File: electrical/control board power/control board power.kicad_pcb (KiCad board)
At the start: 2 copper layers, 147.3 x 147.3 mm, 67 parts, among them J1 Conn_01x02, J10 48V_from_conversion, J11 Aux_2, J17 Switch_B, J2 5V, J3 Barrel_Jack, J4 Switch_A, J5 Switch_Input, J6 Power_Connector, J7 Switch_A_High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

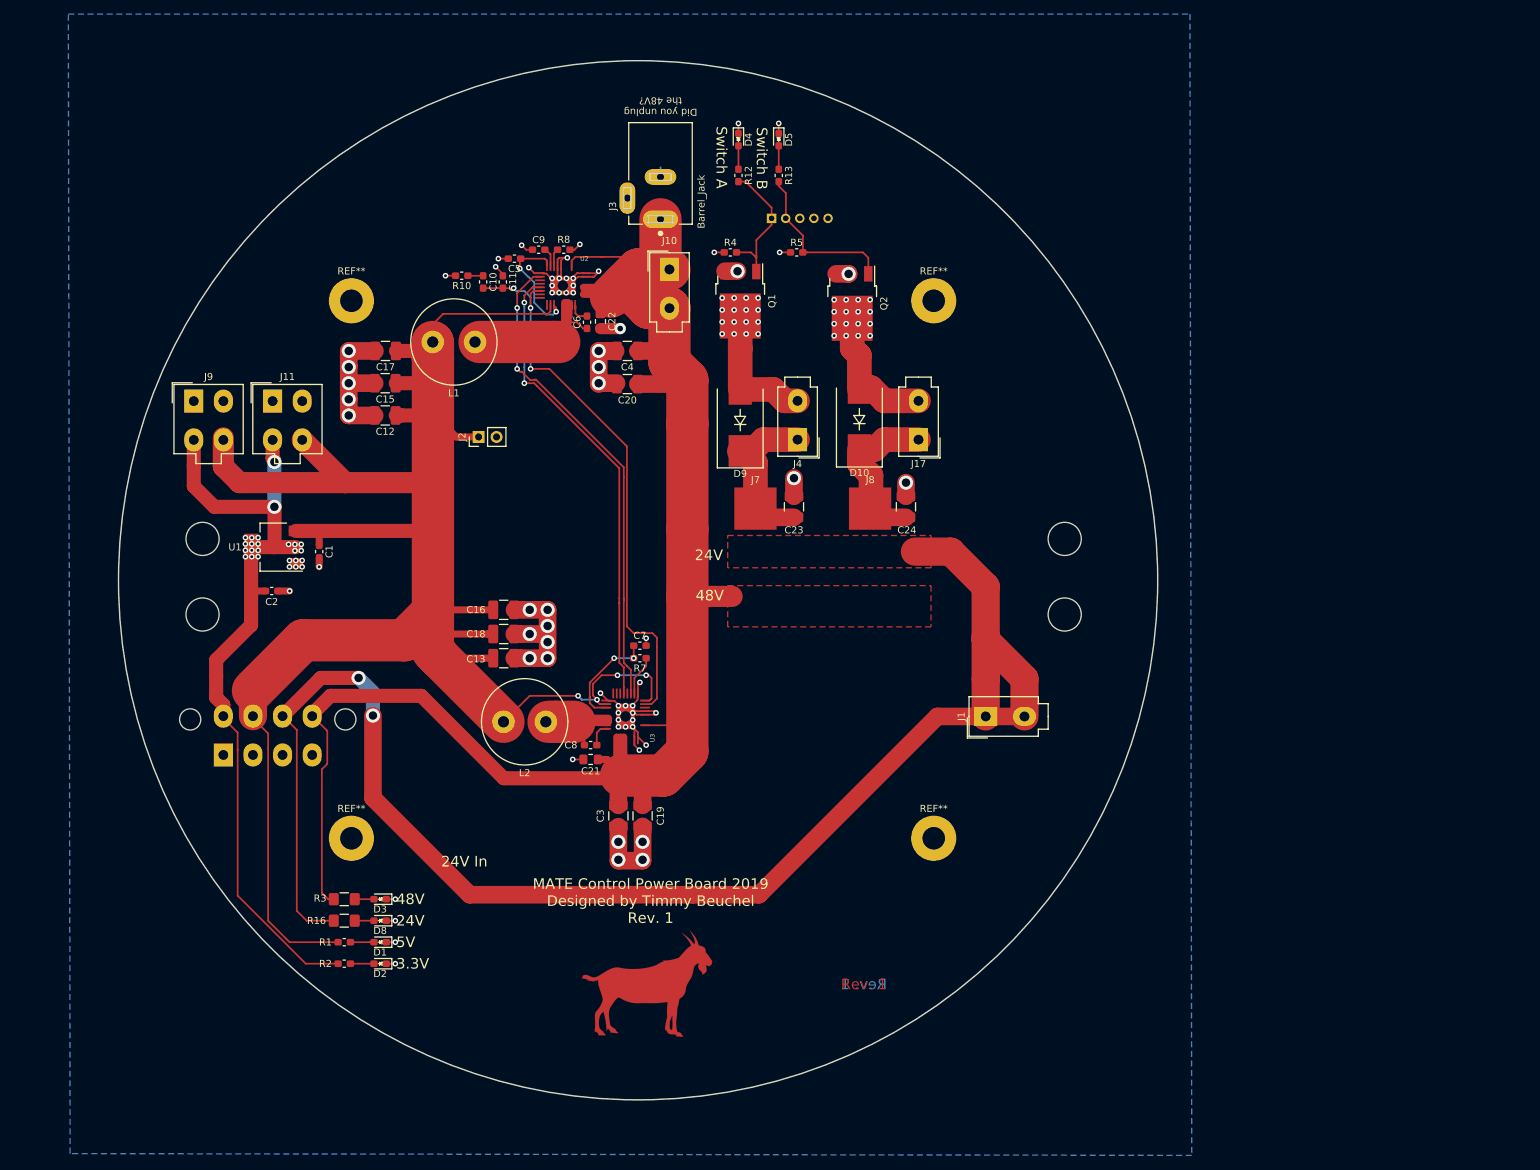
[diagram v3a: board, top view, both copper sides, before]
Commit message: odroid footprint now has correct pad dimentions
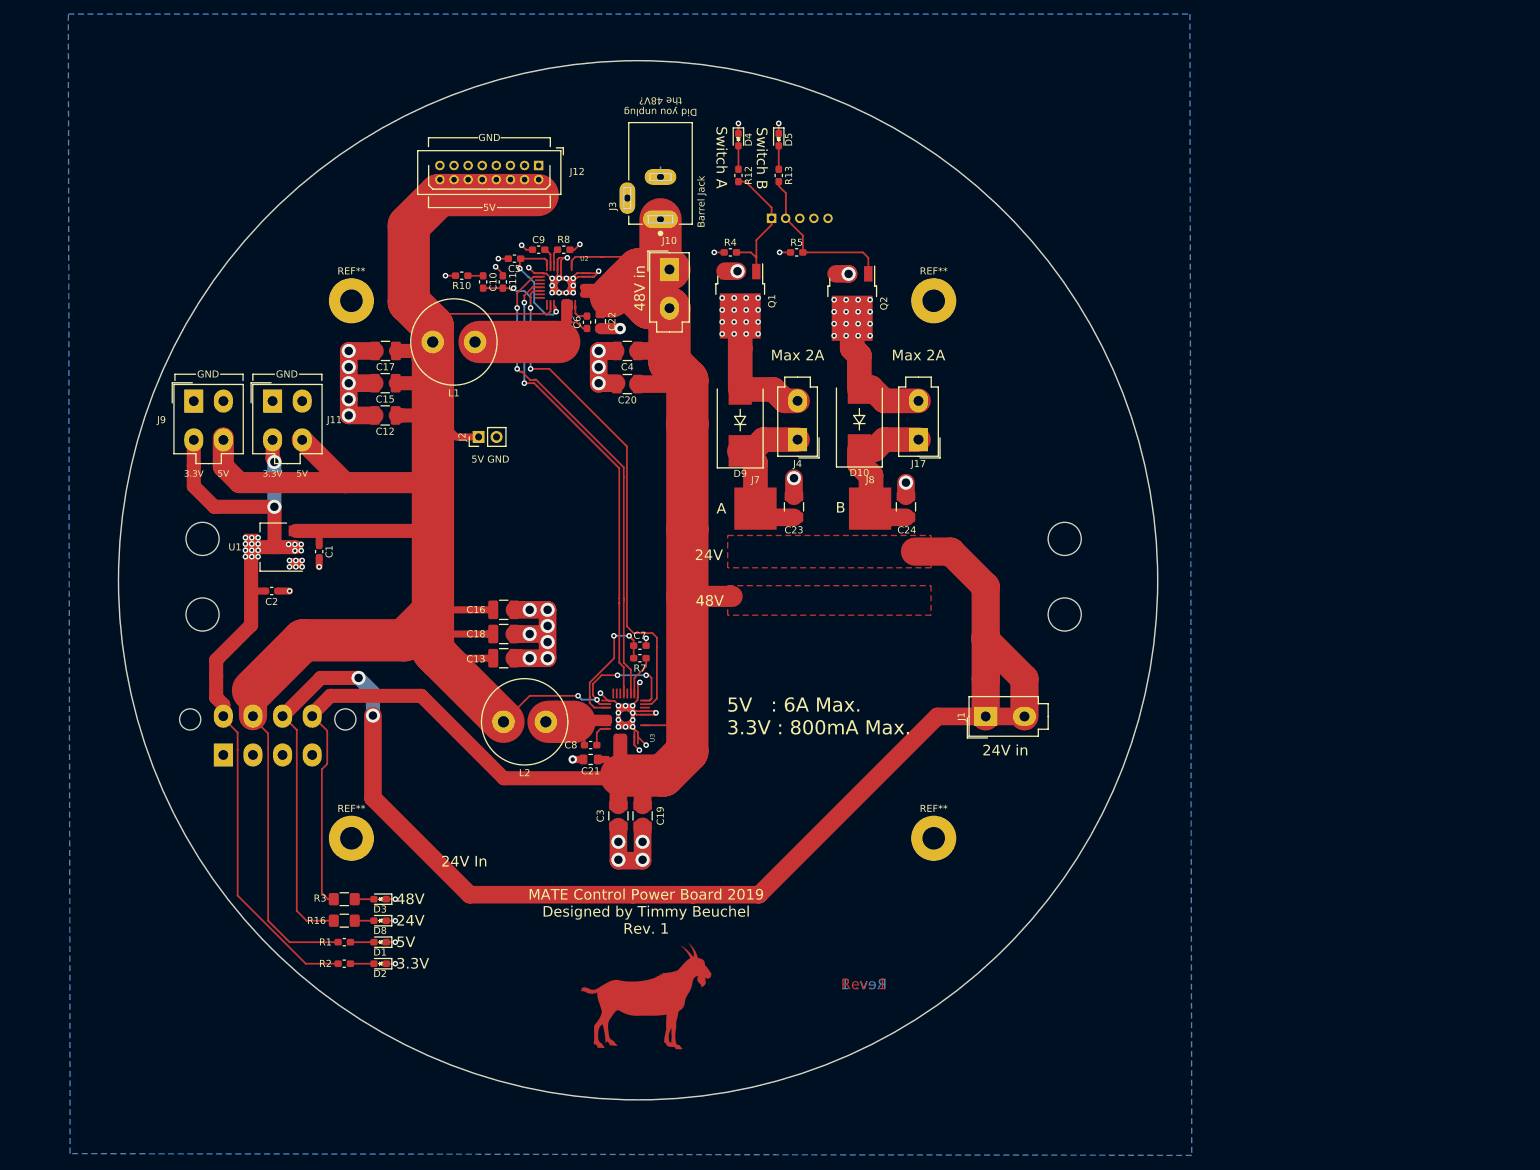
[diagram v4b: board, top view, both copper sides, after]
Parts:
- added J12: Conn_02x08_Odd_Even, Connector_Harwin:Harwin_LTek-Male_2x08_P2.00mm_Vertical, F.Cu at (87.5, 43.6)
- J3: value Barrel_Jack -> Barrel Jack
- moved G*** 1.78 mm to (102.7, 161.3)
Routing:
- net +5V: track 289.0 -> 327.0 mm
- net Net-(C7-Pad1): track 15.5 -> 19.7 mm
- net +3V3: track 114.0 -> 113.4 mm
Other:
- board text added: "24V in"
- board text added: "48V in"
- board text added: "5V : 6A Max. 3.3V : 800mA Max."
- board text added: "A"
- board text added: "B"
- board text added: "Max 2A"
- board text added: "Switch Connector"

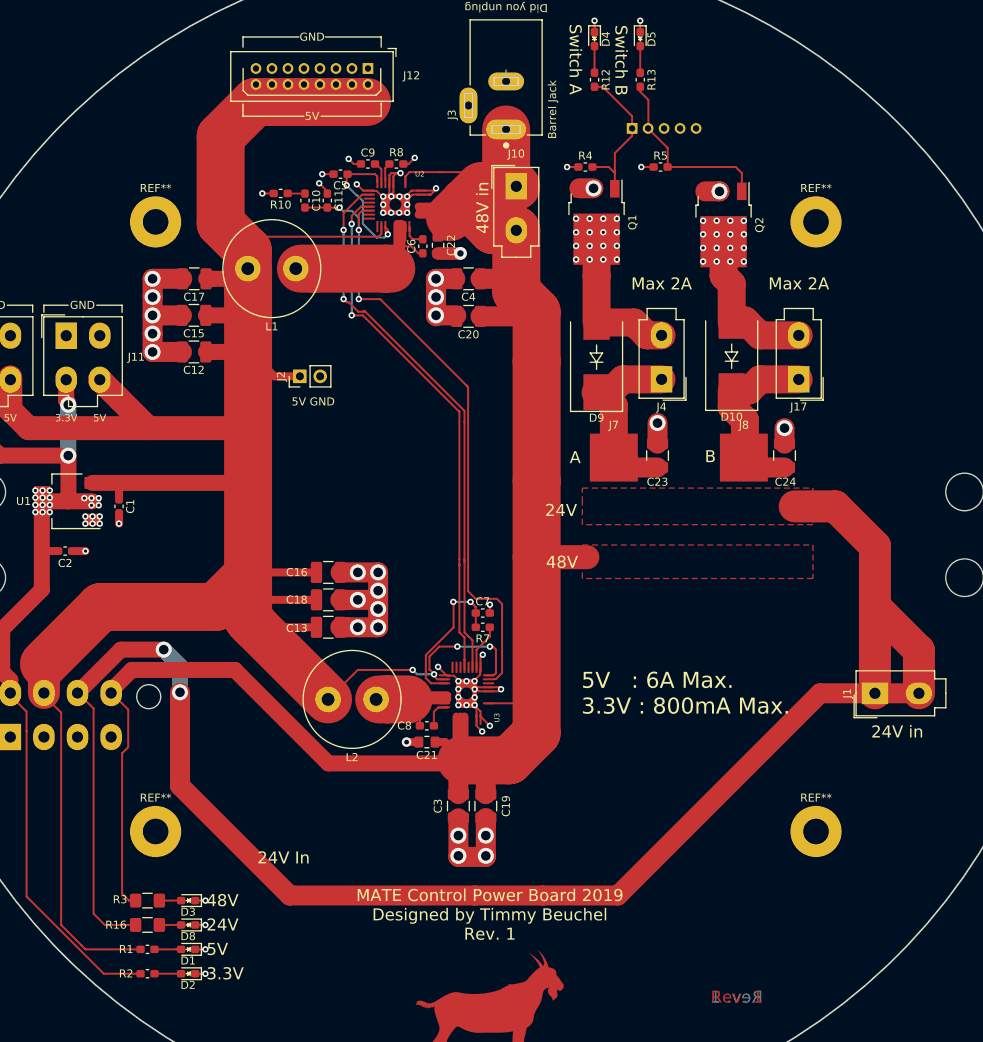
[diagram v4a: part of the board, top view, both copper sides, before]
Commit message: Removed current measurement from power board
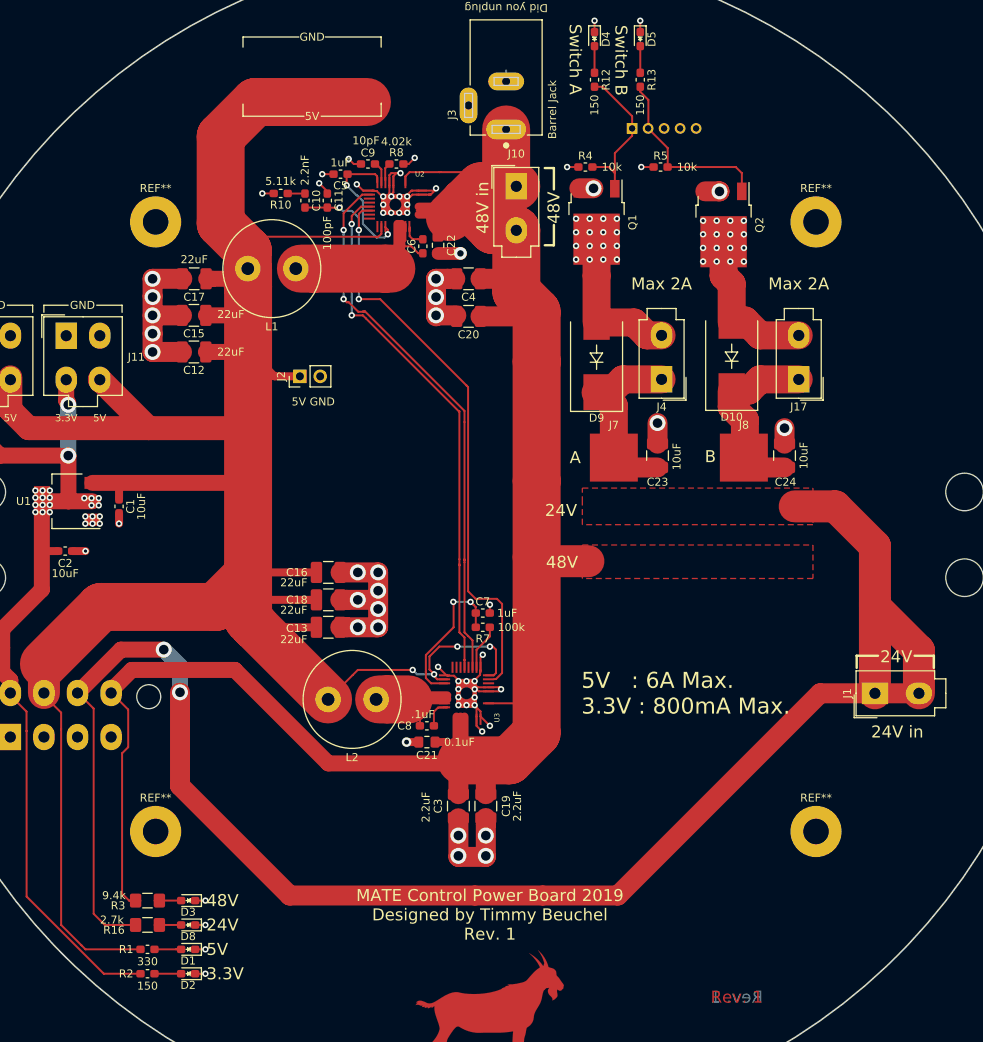
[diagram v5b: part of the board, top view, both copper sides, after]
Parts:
- removed J12: Conn_02x08_Odd_Even, Connector_Harwin:Harwin_LTek-Male_2x08_P2.00mm_Vertical
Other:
- board text removed: "24V In"

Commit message: Lots of important stuff
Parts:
- added C14: 330u, Capacitor_THT:CP_Radial_D18.0mm_P7.50mm, F.Cu at (81.5, 83.5)
- added C25: 330u, Capacitor_THT:CP_Radial_D18.0mm_P7.50mm, F.Cu at (81.2, 140.2)
- added C26: 330u, Capacitor_THT:CP_Radial_D18.0mm_P7.50mm, F.Cu at (127.8, 130.2)
- added C27: 330u, Capacitor_THT:CP_Radial_D18.0mm_P7.50mm, F.Cu at (92.1, 41.7)
- J3: value Barrel Jack -> Barrel_Jack
- J5: value Switch_Input -> Conn_01x03; footprint Connector_Harwin:Harwin_LTek-Male_05_P2.00mm_Vertical -> Connector_Harwin:Harwin_LTek-Male_03_P2.00mm_Vertical; moved to F.Cu
- J6: moved to F.Cu
- moved J2 33.5 mm to (61.6, 53.5), turned to 270 degrees
- moved J6 10.6 mm to (32.3, 128.3), turned to 180 degrees
- moved R13 8.70 mm to (120.2, 36.4), turned to 0 degrees
- moved D5 7.35 mm to (115.1, 36.4), turned to 0 degrees
- moved G*** 6.43 mm to (108.8, 163.5)
- moved R12 5.20 mm to (120.2, 42.1), turned to 0 degrees
- moved D4 2.33 mm to (115.1, 42.1), turned to 0 degrees
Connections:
- J5 pad 3: Net-(J5-Pad3) -> GND
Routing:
- net +3V3: track 113.4 -> 176.8 mm, vias 19 -> 21
- net +5V: track 327.0 -> 298.6 mm
- net +48V: track 234.6 -> 256.4 mm
- net /SWITCH_B: track 23.4 -> 33.6 mm
- net +24V: track 218.9 -> 226.3 mm
- net Net-(C7-Pad1): track 19.7 -> 15.9 mm
- net Net-(C8-Pad2): track 14.6 -> 11.9 mm
- net /SWITCH_A: track 19.4 -> 20.8 mm

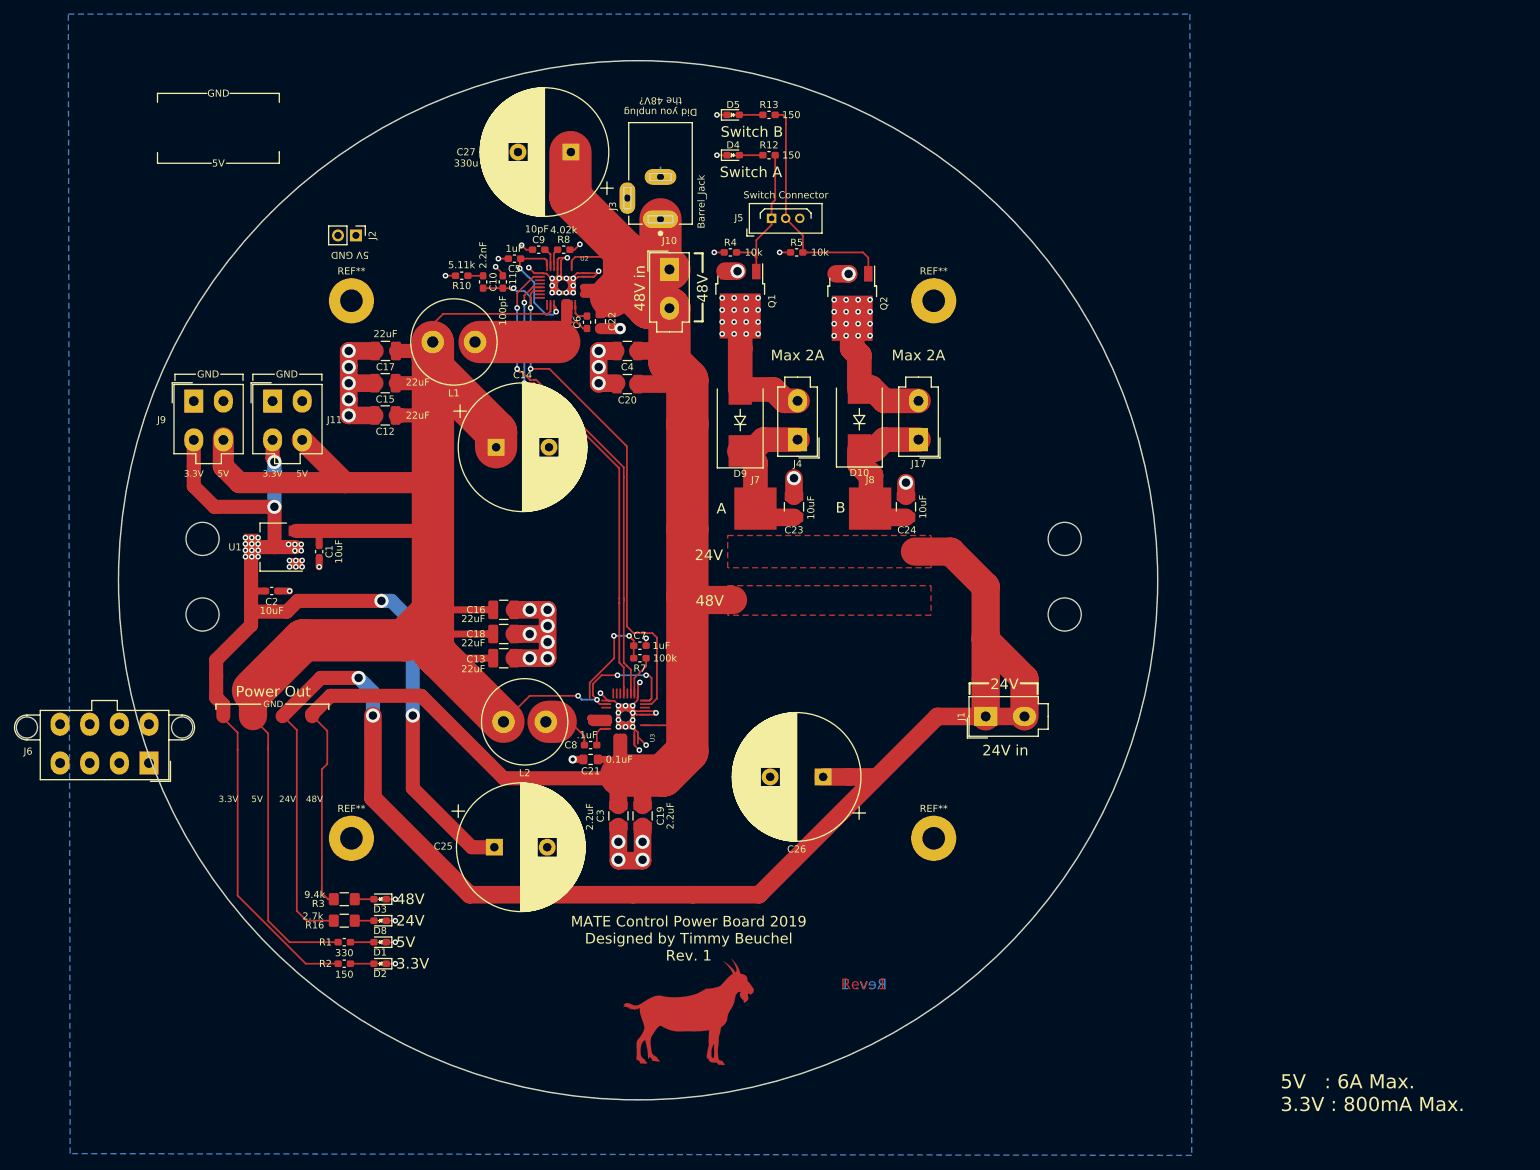
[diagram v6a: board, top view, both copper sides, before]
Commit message: Added cutout for cables to pass by
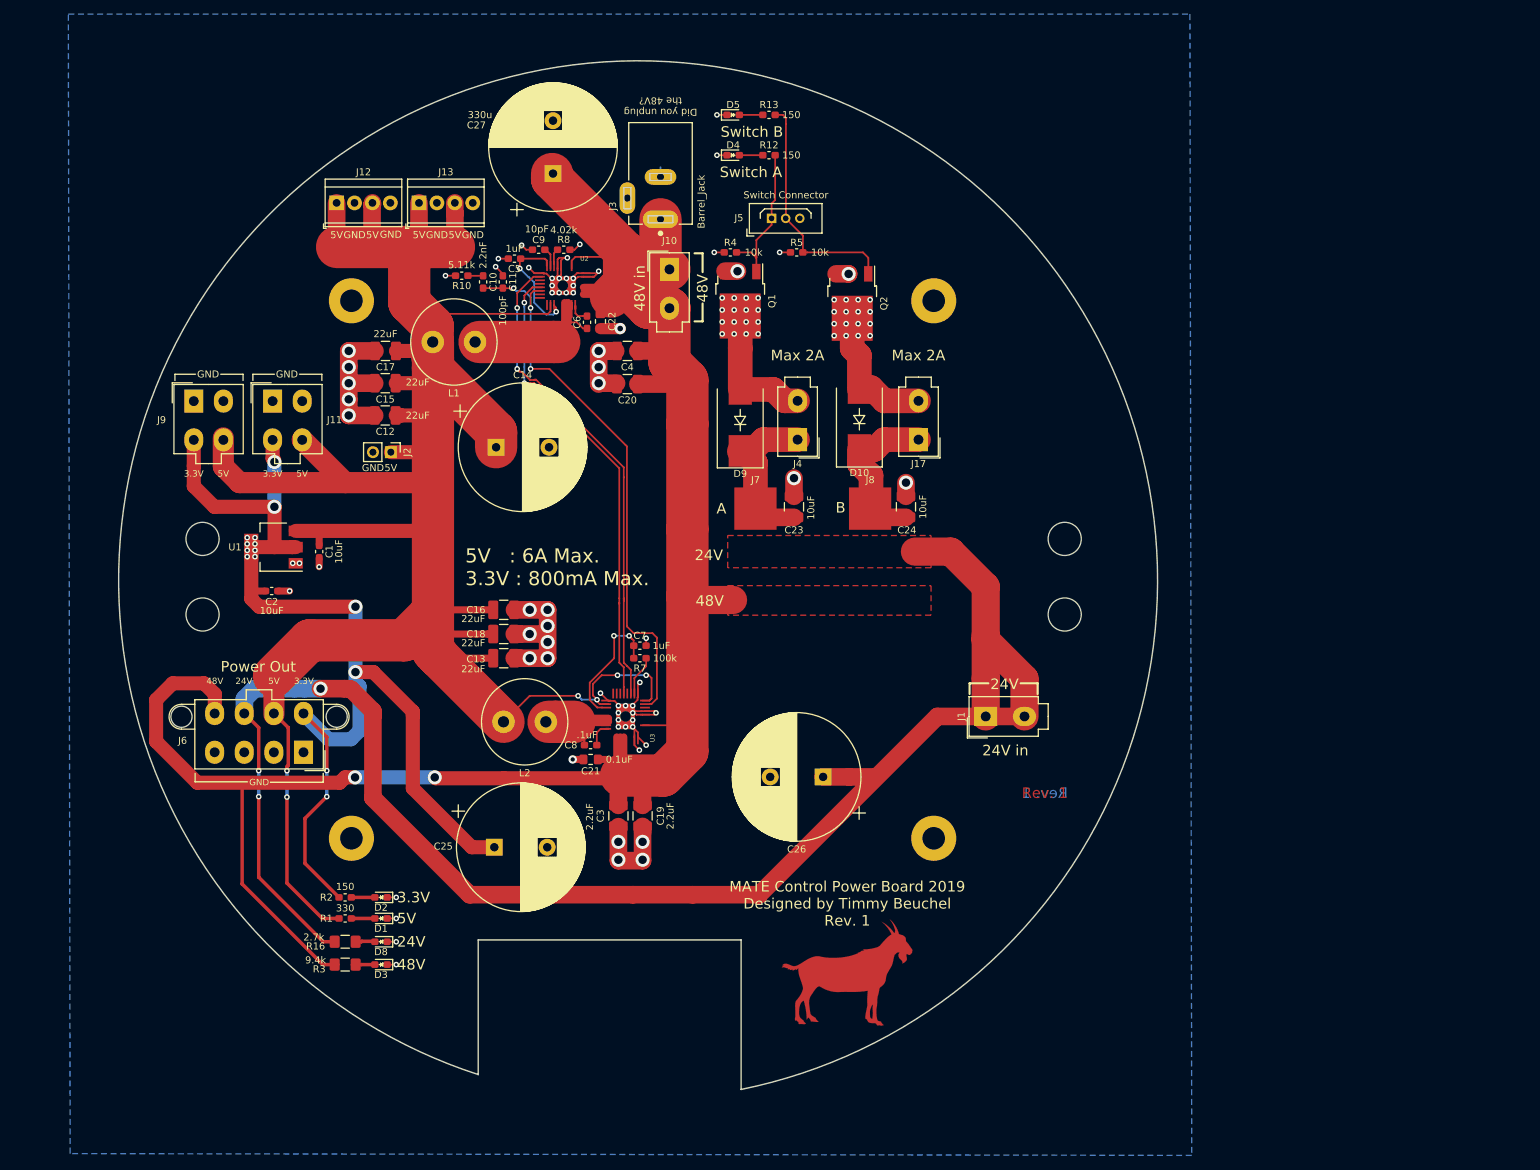
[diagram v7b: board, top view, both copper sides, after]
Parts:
- added J12: Conn_01x04, TerminalBlock_TE-Connectivity:TerminalBlock_TE_282834-4_1x04_P2.54mm_Horizontal, F.Cu at (58.9, 48.9)
- added J13: Conn_01x04, TerminalBlock_TE-Connectivity:TerminalBlock_TE_282834-4_1x04_P2.54mm_Horizontal, F.Cu at (70.5, 48.9)
- moved J2 31.1 mm to (66.5, 84.2)
- moved G*** 23.2 mm to (131.3, 157.9)
- moved J6 22.0 mm to (54.2, 126.7)
- moved D2 9.40 mm to (65.2, 147.3)
- moved R2 9.40 mm to (60.1, 147.3)
- moved D3 9.27 mm to (65.2, 156.8)
- moved R3 9.27 mm to (60.1, 156.8)
- moved C27 3.97 mm to (89.5, 44.7), turned to 90 degrees
- moved D1 3.37 mm to (65.2, 150.3)
- moved R1 3.37 mm to (60.1, 150.3)
- moved D8 2.99 mm to (65.2, 153.6)
- moved R16 2.99 mm to (60.1, 153.6)
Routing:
- net +5V: track 298.6 -> 349.2 mm, vias 4 -> 6
- net +48V: track 256.4 -> 295.6 mm, vias 0 -> 2
- net +3V3: track 176.8 -> 159.3 mm, vias 21 -> 14
- net +24V: track 226.3 -> 233.7 mm, vias 2 -> 3
- net Net-(C8-Pad2): track 11.9 -> 14.6 mm
- net Net-(C7-Pad1): track 15.9 -> 18.4 mm
- net GND: vias 75 -> 71
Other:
- board size 147.3 x 147.3 mm -> 147.3 x 145.8 mm
